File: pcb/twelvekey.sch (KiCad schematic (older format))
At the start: 39 parts, among them J1 Conn_01x06, U1 ATmega328P-AU, U2 SRV05-4, X1 Crystal_GND24_Small

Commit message: updated PCB to support per-key LEDs
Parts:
- removed MX1, MX10, MX11, MX12, MX2, MX3, MX4, MX5, MX6, MX7, MX8, MX9: MX-NoLED, MX_Only:MXOnly-1U-NoLED, symbol MX_Alps_Hybrid:MX-NoLED
- added MX1, MX10, MX11, MX12, MX2, MX3, MX4, MX5, MX6, MX7, MX8, MX9: MX-LED, MX_Only:MXOnly-1U, symbol MX_Alps_Hybrid:MX-LED
- added Q1: AO3401A, Package_TO_SOT_SMD:SOT-23, symbol Transistor_FET:AO3401A
- added R1, R10, R11, R12, R13, R14, R15, R16, R17, R18, R3, R4: 1k, Resistor_SMD:R_0805_2012Metric, symbol Device:R_Small
- added R19: 100r, Resistor_SMD:R_0805_2012Metric, symbol Device:R_Small
- added R20: 10k, Resistor_SMD:R_0805_2012Metric, symbol Device:R_Small
- D1, D2, D3, D4, D5, D6: LCSC C81598 -> C68978
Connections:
- net +5V: now also Q1.3 (D), R20.1
- net GND: now also R1.2, R10.2, R11.2, R12.2, R13.2, R14.2, R15.2, R16.2, R17.2, R18.2, R3.2, R4.2
- net col0: now also U1.28 (PC5), MX1.1 (COL), MX5.1 (COL), MX9.1 (COL); no longer U1.24 (PC1)
- net col1: now also U1.30 (PD0), MX10.1 (COL), MX2.1 (COL), MX6.1 (COL); no longer U1.26 (PC3)
- net col2: now also U1.12 (PB0), MX11.1 (COL), MX3.1 (COL), MX7.1 (COL); no longer U1.14 (PB2)
- net col3: now also U1.10 (PD6), MX12.1 (COL), MX4.1 (COL), MX8.1 (COL); no longer U1.13 (PB1)
- net row0: now also U1.31 (PD1); no longer U1.27 (PC4)
- net row1: now also U1.27 (PC4); no longer U1.25 (PC2)
- net row2: now also U1.11 (PD7); no longer U1.23 (PC0)
- net at D1.2 (A): now also MX1.2 (ROW), MX2.2 (ROW)
- net at D2.2 (A): now also MX3.2 (ROW), MX4.2 (ROW)
- net at D3.2 (A): now also MX5.2 (ROW), MX6.2 (ROW)
- net at D4.2 (A): now also MX7.2 (ROW), MX8.2 (ROW)
- net at U1.9 (PD5): now also R19.2, R20.2
- net at D6.2 (A): now also MX11.2 (ROW), MX12.2 (ROW)
- net at D5.2 (A): now also MX10.2 (ROW), MX9.2 (ROW)
- new net: MX1.4 (LEDGND), R1.1
- new net: MX2.4 (LEDGND), R3.1
- new net: MX3.4 (LEDGND), R4.1
- new net: MX4.4 (LEDGND), R10.1
- new net: MX8.4 (LEDGND), R14.1
- new net: MX7.4 (LEDGND), R13.1
- new net: MX6.4 (LEDGND), R12.1
- new net: MX5.4 (LEDGND), R11.1
- new net: MX9.4 (LEDGND), R15.1
- new net: MX10.4 (LEDGND), R16.1
- new net: MX11.4 (LEDGND), R17.1
- new net: MX12.4 (LEDGND), R18.1
- new net: Q1.1 (G), R19.1
- new net LED+: MX1.3 (LED), MX10.3 (LED), MX11.3 (LED), MX12.3 (LED), MX2.3 (LED), MX3.3 (LED), MX4.3 (LED), MX5.3 (LED), MX6.3 (LED), MX7.3 (LED), MX8.3 (LED), MX9.3 (LED), Q1.2 (S)

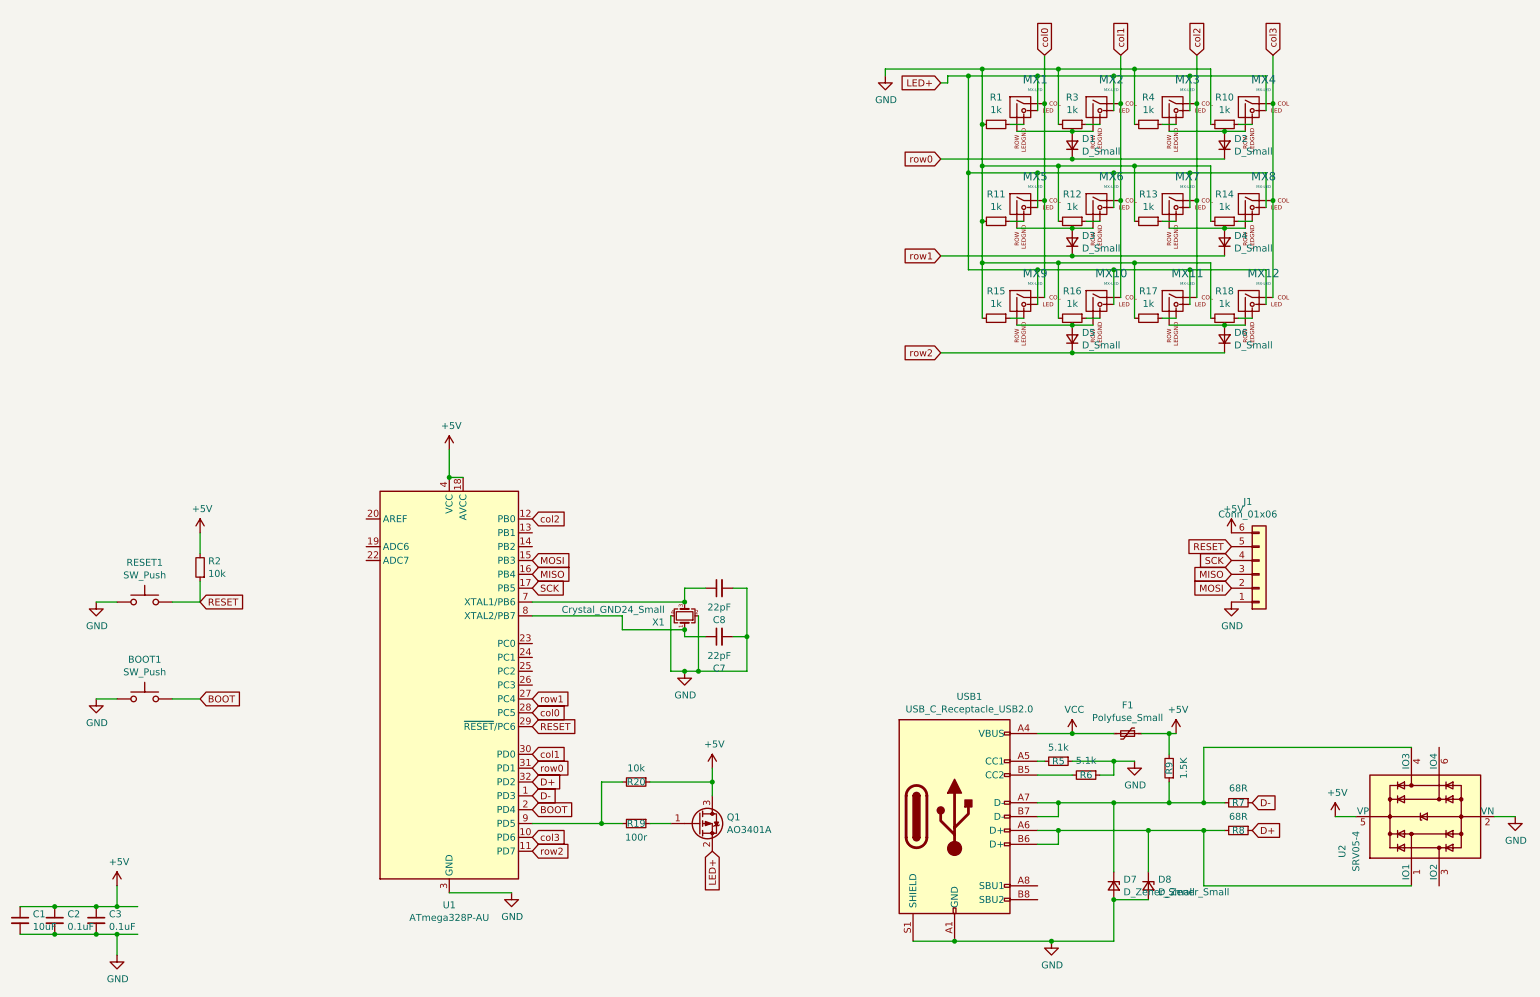
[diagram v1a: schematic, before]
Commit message: fix backlight
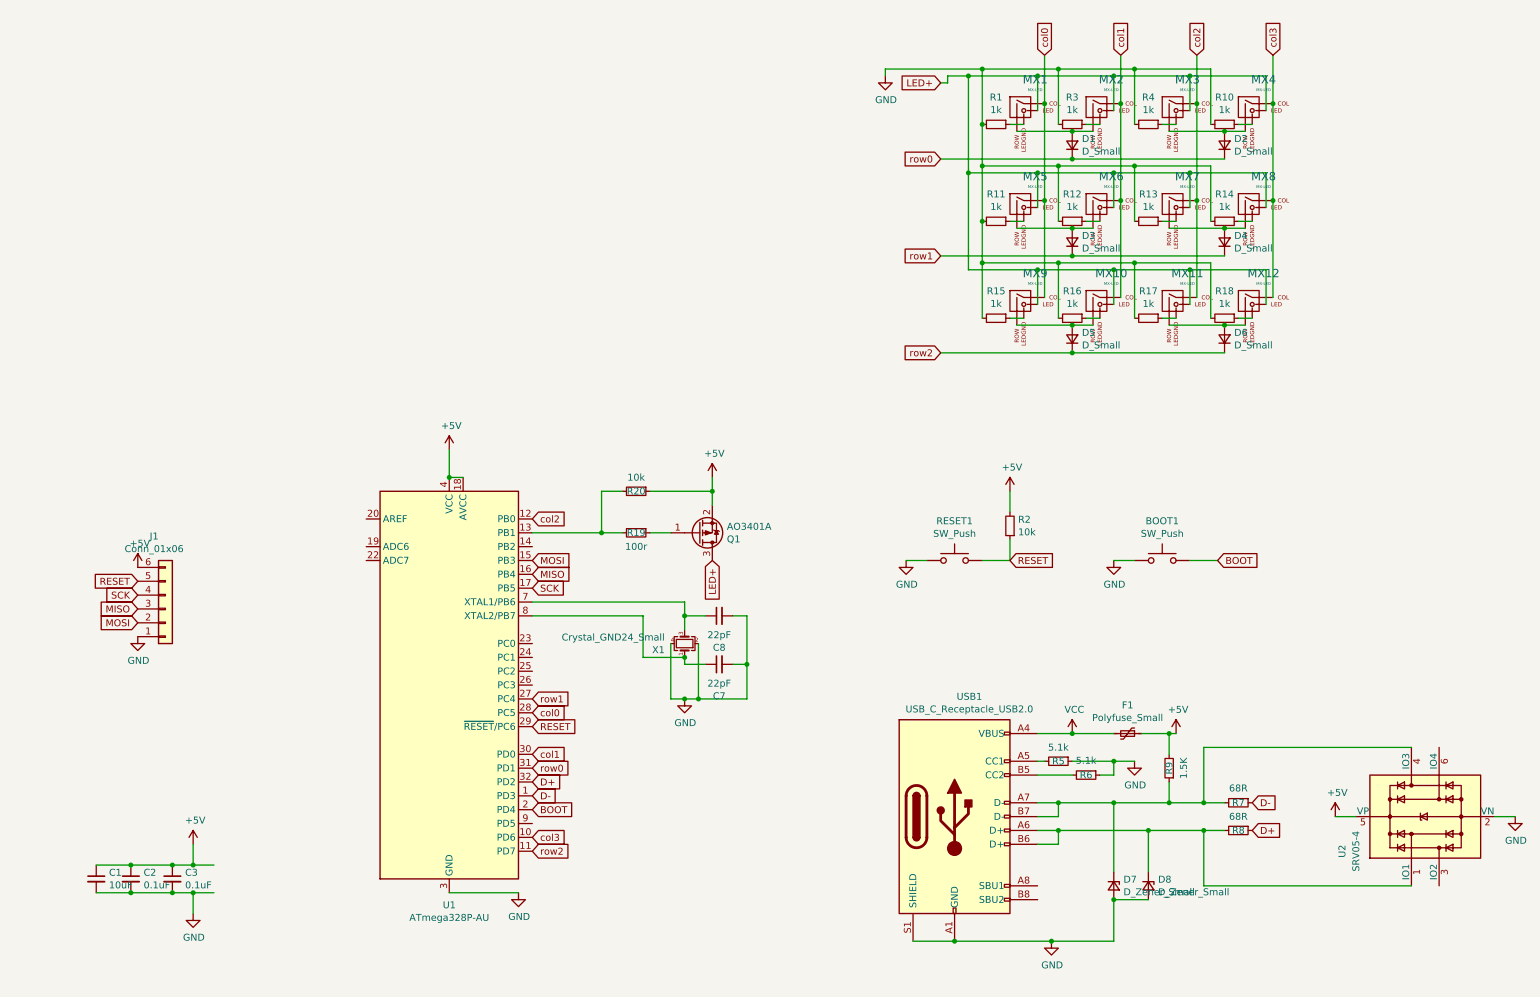
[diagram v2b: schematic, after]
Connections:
- net +5V: now also Q1.2 (S); no longer Q1.3 (D)
- net LED+: now also Q1.3 (D); no longer Q1.2 (S)
- net at U1.13 (PB1): now also R19.2, R20.2
- now unconnected: U1.9 (PD5)
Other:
- moved on the sheet: BOOT1, C1, C2, C3, C7, C8, J1, Q1, R19, R2, R20, RESET1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
